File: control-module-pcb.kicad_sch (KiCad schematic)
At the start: 0 parts

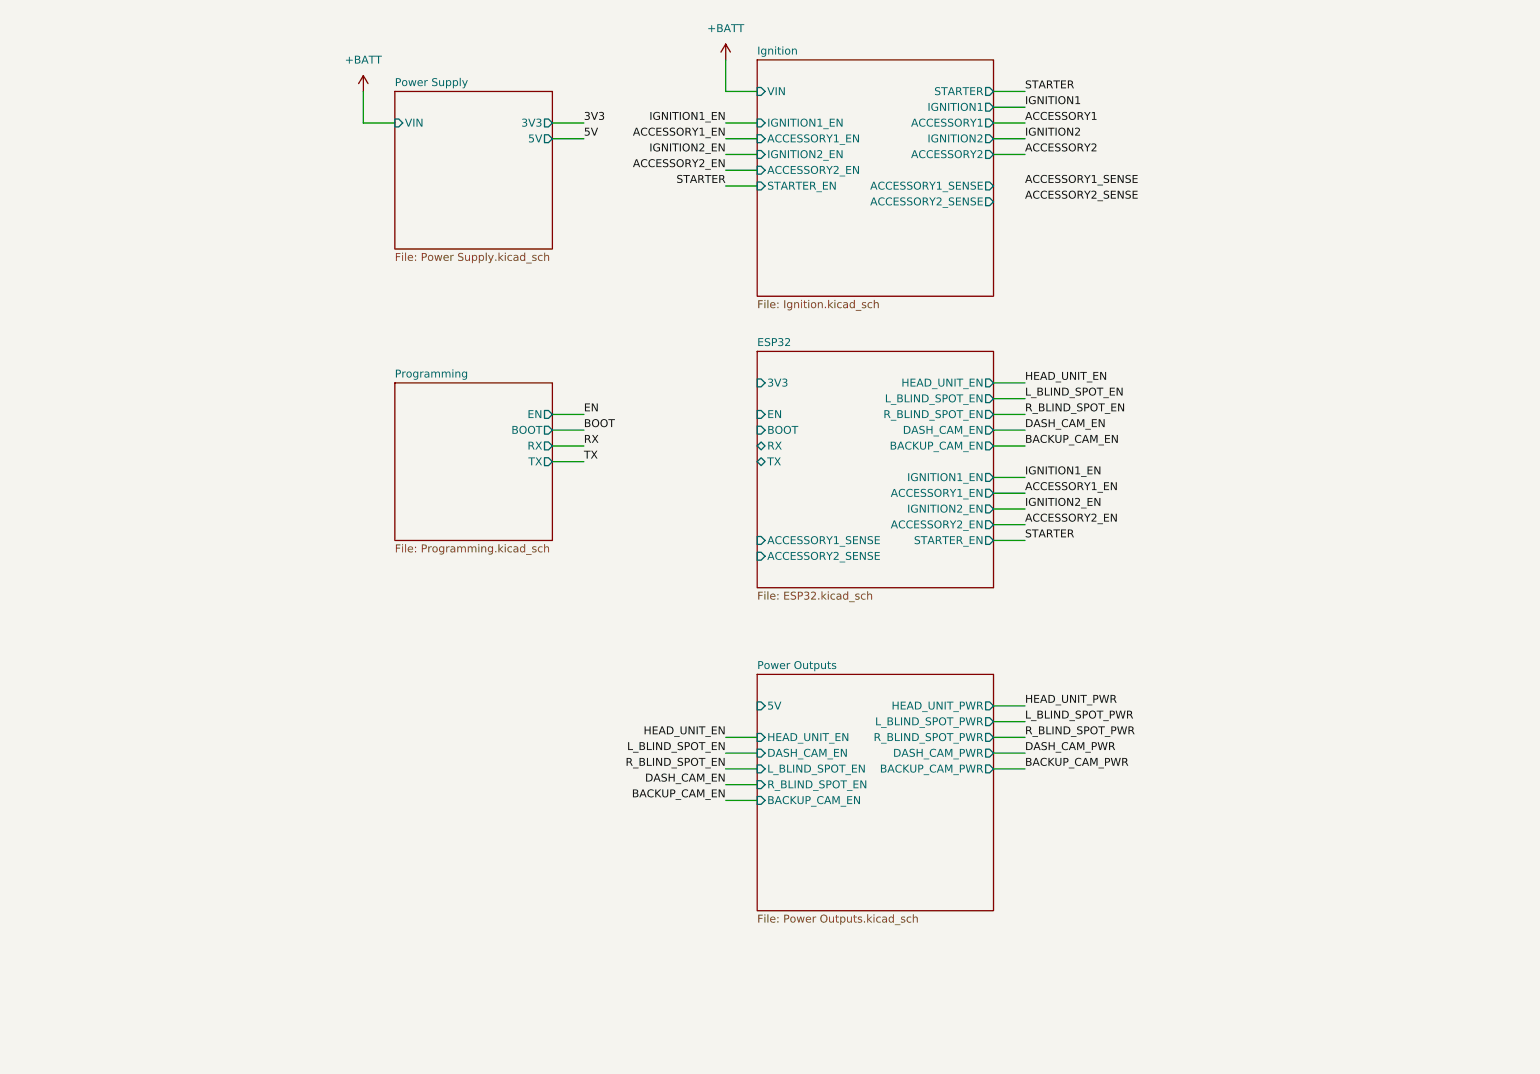
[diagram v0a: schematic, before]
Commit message: power supply circuit schematic done
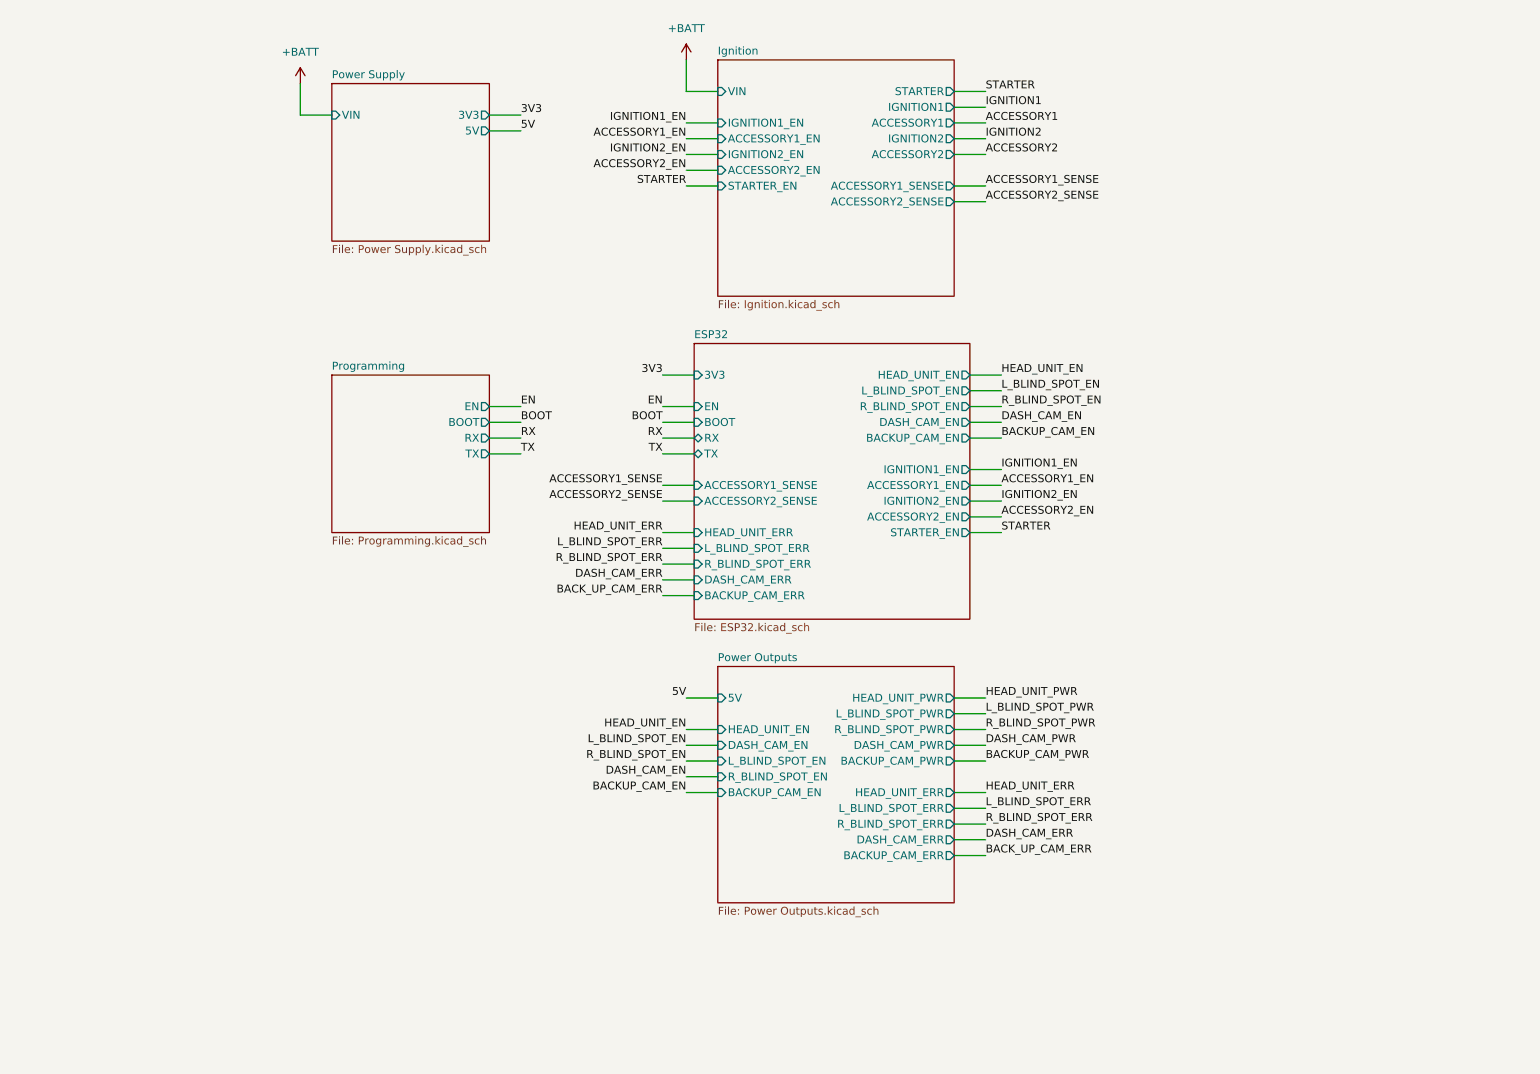
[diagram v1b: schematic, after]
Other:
- sheet ESP32 ports: added BACKUP_CAM_ERR, DASH_CAM_ERR, HEAD_UNIT_ERR, L_BLIND_SPOT_ERR, R_BLIND_SPOT_ERR; removed none
- sheet Power Outputs ports: added BACKUP_CAM_ERR, DASH_CAM_ERR, HEAD_UNIT_ERR, L_BLIND_SPOT_ERR, R_BLIND_SPOT_ERR; removed none

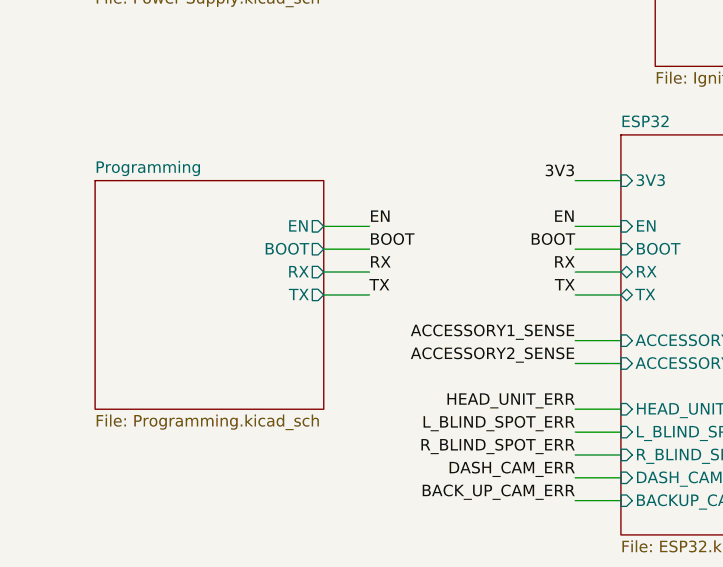
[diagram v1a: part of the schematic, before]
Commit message: working on ignition and power output sheets
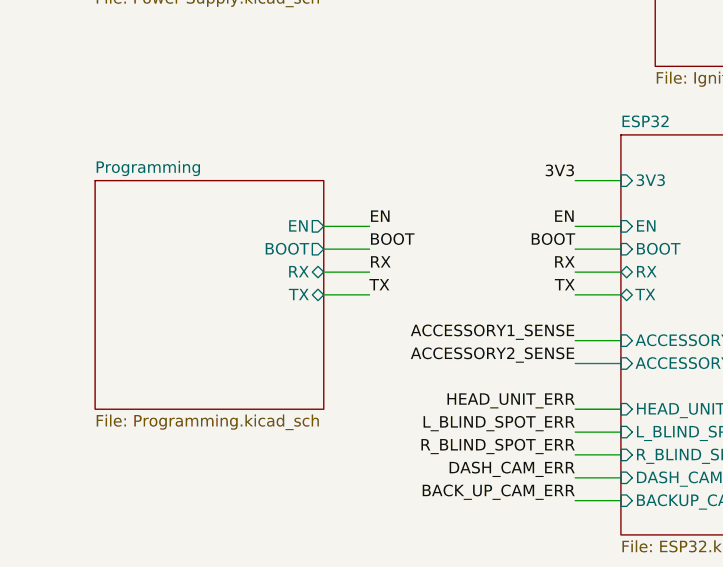
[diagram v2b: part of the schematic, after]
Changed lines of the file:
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@@
       (effects (font (size 1.27 1.27)) (justify left top))
     )
-    (pin "EN" output (at 92.71 83.82 0)
+    (pin "TX" bidirectional (at 92.71 91.44 0)
+      (effects (font (size 1.27 1.27)) (justify right))
+    )
+    (pin "RX" bidirectional (at 92.71 88.9 0)
       (effects (font (size 1.27 1.27)) (justify right))
     )
@@
       (effects (font (size 1.27 1.27)) (justify right))
     )
-    (pin "RX" output (at 92.71 88.9 0)
+    (pin "EN" output (at 92.71 83.82 0)
       (effects (font (size 1.27 1.27)) (justify right))
     )
-    (pin "TX" output (at 92.71 91.44 0)
-      (effects (font (size 1.27 1.27)) (justify right))
-    )

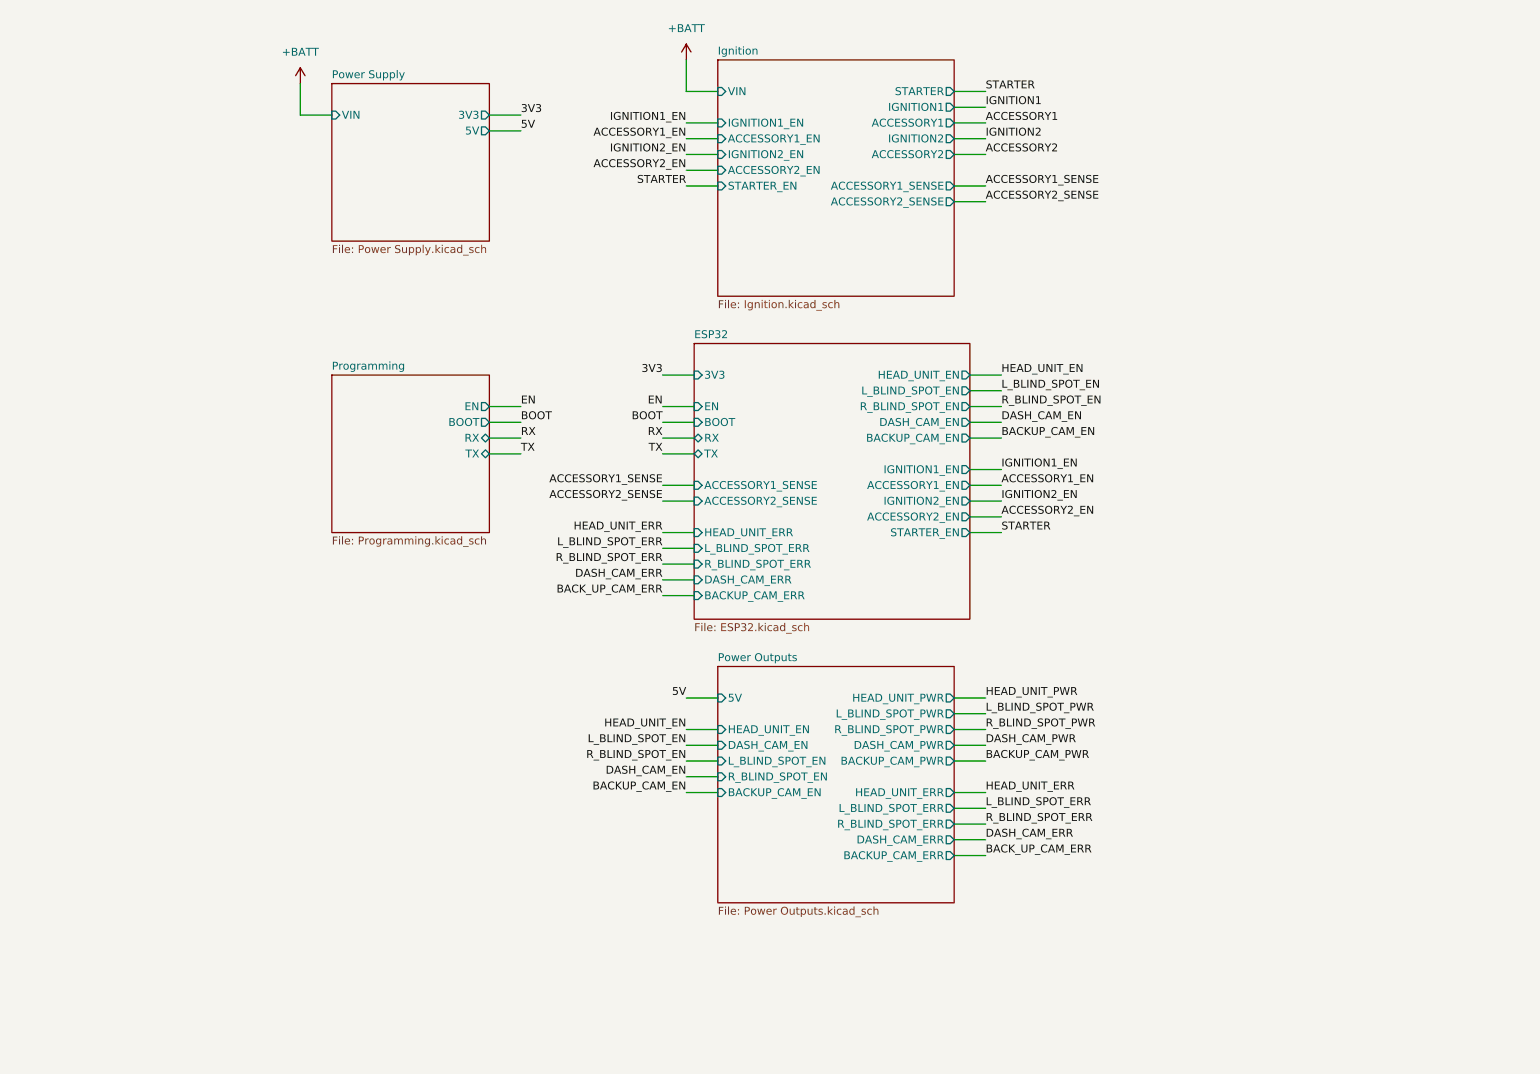
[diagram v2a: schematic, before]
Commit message: switch Ignition page to use load drivers rather than discrete FETs
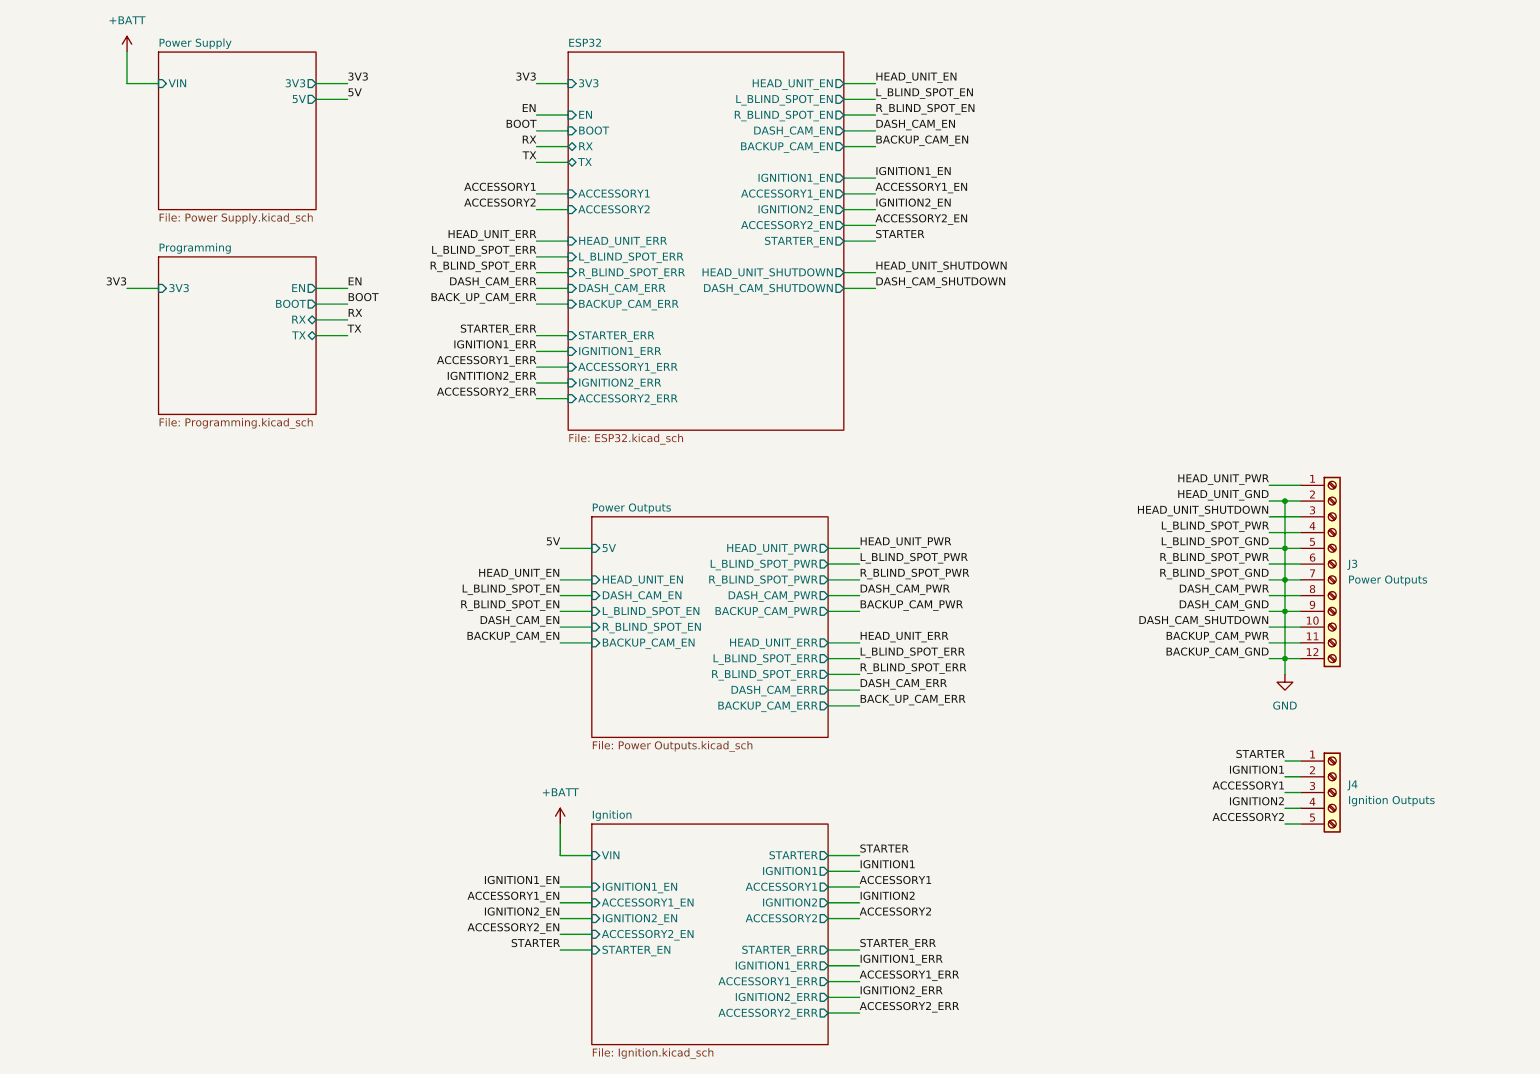
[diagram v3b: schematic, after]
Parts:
- added J3: Power Outputs, symbol Connector:Screw_Terminal_01x12
- added J4: Ignition Outputs, symbol Connector:Screw_Terminal_01x05
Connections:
- net ACCESSORY1: now also J4.3 (Pin_3)
- net ACCESSORY2: now also J4.5 (Pin_5)
- net BACKUP_CAM_PWR: now also J3.11 (Pin_11)
- net DASH_CAM_PWR: now also J3.8 (Pin_8)
- net HEAD_UNIT_PWR: now also J3.1 (Pin_1)
- net IGNITION1: now also J4.2 (Pin_2)
- net IGNITION2: now also J4.4 (Pin_4)
- net L_BLIND_SPOT_PWR: now also J3.4 (Pin_4)
- net R_BLIND_SPOT_PWR: now also J3.6 (Pin_6)
- net STARTER: now also J4.1 (Pin_1)
- new net DASH_CAM_SHUTDOWN: J3.10 (Pin_10)
- new net GND: J3.12 (Pin_12), J3.2 (Pin_2), J3.5 (Pin_5), J3.7 (Pin_7), J3.9 (Pin_9)
- new net HEAD_UNIT_SHUTDOWN: J3.3 (Pin_3)
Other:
- sheet ESP32 ports: added ACCESSORY1, ACCESSORY1_ERR, ACCESSORY2, ACCESSORY2_ERR, DASH_CAM_SHUTDOWN, HEAD_UNIT_SHUTDOWN, IGNITION1_ERR, IGNITION2_ERR, STARTER_ERR; removed ACCESSORY1_SENSE, ACCESSORY2_SENSE
- sheet Ignition ports: added ACCESSORY1_ERR, ACCESSORY2_ERR, IGNITION1_ERR, IGNITION2_ERR, STARTER_ERR; removed ACCESSORY1_SENSE, ACCESSORY2_SENSE
- sheet Programming ports: added 3V3; removed none
- company: (none) -> J2B

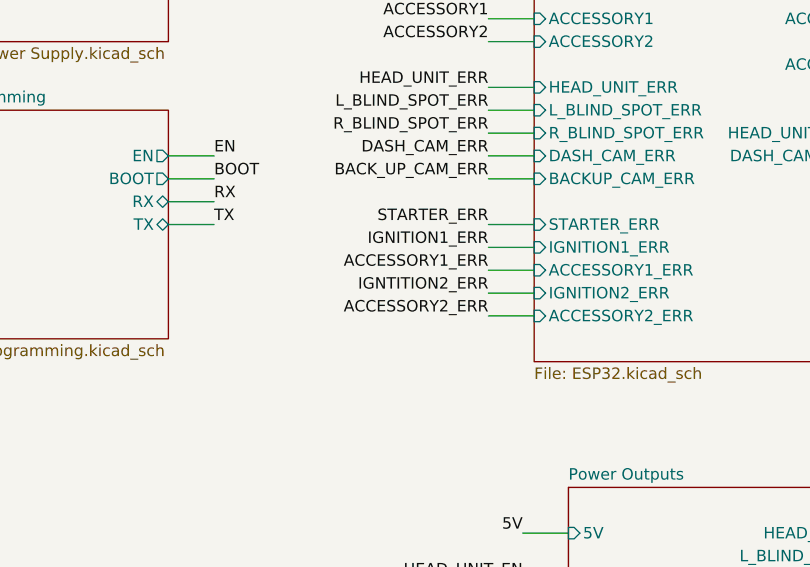
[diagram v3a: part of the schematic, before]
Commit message: fix ERC errors
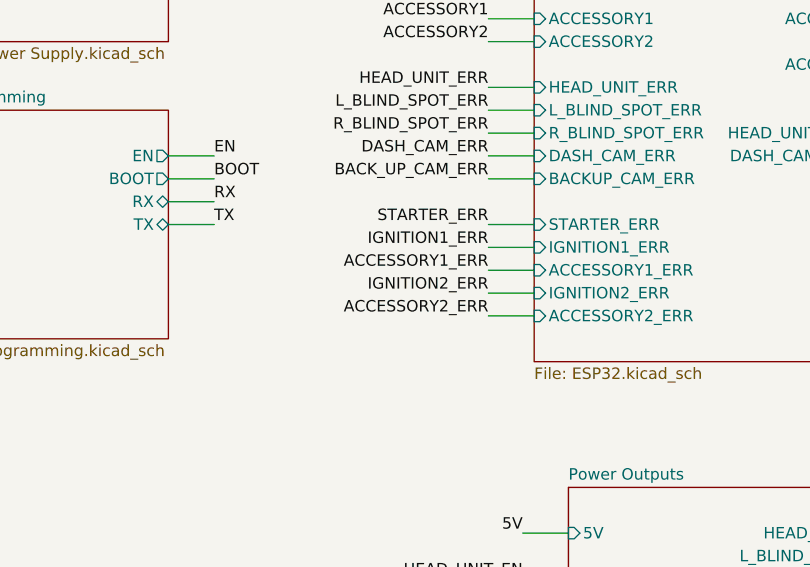
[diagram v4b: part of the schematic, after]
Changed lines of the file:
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@@
     (effects (font (size 1.27 1.27)) (justify left bottom))
   )
-  (label "IGNTITION2_ERR" (at 100.33 80.01 180) (fields_autoplaced)
+  (label "IGNITION2_ERR" (at 100.33 80.01 180) (fields_autoplaced)
     (effects (font (size 1.27 1.27)) (justify right bottom))
   )
